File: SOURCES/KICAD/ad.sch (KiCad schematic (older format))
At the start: 178 parts, among them IC201 IC_OPA1652AIDR, IC202 IC_OPA1652AIDR, IC203 IC_OPA1652AIDR, IC204 IC_OPA1652AIDR, IC205 IC_AK5558VN, IC206 IC_OPA1652AIDR, IC207 IC_OPA1652AIDR, IC208 IC_OPA1652AIDR, IC209 IC_OPA1652AIDR, X201 CONN_02X13

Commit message: I2C control of ADC
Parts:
- removed R216: RES_0R00_1%_0.125W_Thick_0805, rklib:C0805-RES, symbol rk:RES_0R00_1%_0.125W_Thick_0805
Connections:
- net +3V3: now also IC205.44 (CKS1/CAD0_I2C/CSN), IC205.48 (SD/PMOD), IC205.52 (TDM1), IC205.56 (DCKS/HPFE); no longer IC205.53 (PSN/CAD0_SPI), R213.1, R214.1, R225.1, R226.1
- net GND: now also IC205.46 (CKS3/CAD1), IC205.47 (SLOW/DCKB), IC205.49 (DIF0), IC205.50 (DIF1), IC205.51 (TDM0), IC205.53 (PSN/CAD0_SPI); no longer R215.1, R217.1, R235.2, R236.2, R237.2
- net at R237.1: no longer IC205.43 (CKS0/SDA/CDTI)
- net at R227.2: no longer IC205.44 (CKS1/CAD0_I2C/CSN)
- net at R226.2: no longer IC205.45 (CKS2/SCL/CCLK)
- net at R236.1: no longer IC205.46 (CKS3/CAD1)
- net at R235.1: no longer IC205.47 (SLOW/DCKB)
- net at R225.2: no longer IC205.48 (SD/PMOD)
- net at R217.2: no longer IC205.49 (DIF0)
- net at R215.2: no longer IC205.51 (TDM0)
- net at R214.2: no longer IC205.52 (TDM1)
- net at R213.2: no longer IC205.56 (DCKS/HPFE)
- new net SCL: IC205.45 (CKS2/SCL/CCLK)
- new net SDA: IC205.43 (CKS0/SDA/CDTI)
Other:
- note added: "I2C addr: 0x22/0x23"
- note removed: "Resistors are only for\nprototype"
- moved on the sheet: R213, R214, R215, R217, R225, R226, R235, R236, R237, X201

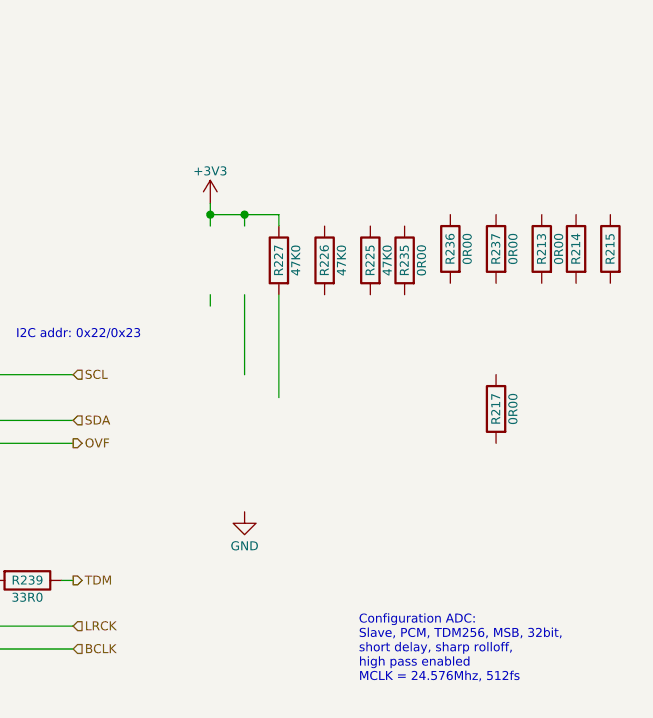
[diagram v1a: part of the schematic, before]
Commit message: I2C control of DAC
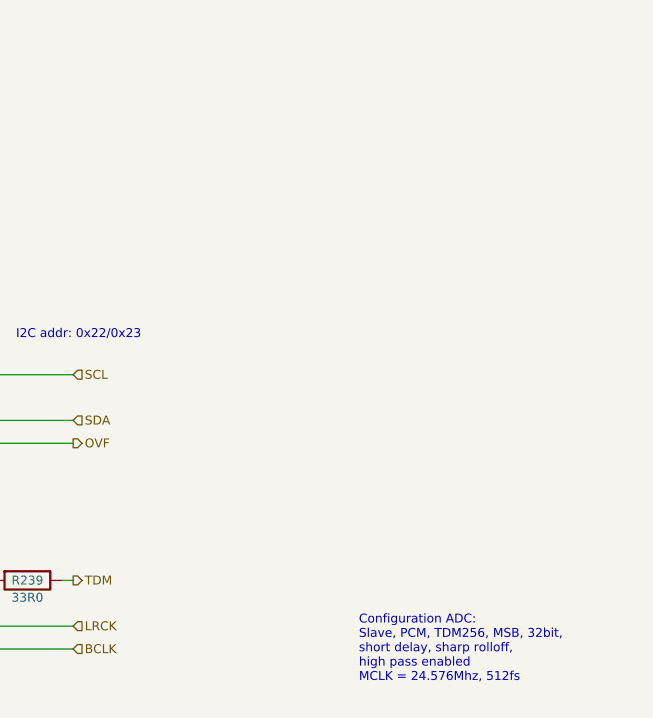
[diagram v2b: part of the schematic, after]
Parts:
- removed R213, R214, R215, R217, R235, R236, R237: RES_0R00_1%_0.125W_Thick_0805, rklib:C0805-RES, symbol rk:RES_0R00_1%_0.125W_Thick_0805
- removed R225, R226, R227: RES_47K0_1%_0.125W_Thick_0805, rklib:C0805-RES, symbol rk:RES_47K0_1%_0.125W_Thick_0805
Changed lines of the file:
@@
 Text HLabel 13250 5400 2    39   Output ~ 0
 OVF
-$Comp
-L freeDSP-aurora-rescue:+3V3 #PWR0135
-U 1 1 59094BBE
-P 13850 4350
-F 0 "#PWR0135" H 13850 4200 50  0001 C CNN
-F 1 "+3V3" H 13850 4490 39  0000 C CNN
-F 2 "" H 13850 4350 50  0000 C CNN
-F 3 "" H 13850 4350 50  0000 C CNN
-	1    13850 4350
-	1    0    0    -1
-$EndComp
 Connection ~ 4400 2000
 Wire Wire Line
@@
 Wire Wire Line
 	12750 5400 13250 5400
-Wire Wire Line
-	13850 4800 13850 4750
-Wire Wire Line
-	13850 4350 13850 4400
-Wire Wire Line
-	13850 4400 14000 4400
-Connection ~ 13850 4400
 Text HLabel 12000 6800 3    39   Input ~ 0
 ~RST
@@
 NoConn ~ 12750 5600
 NoConn ~ 12750 5500
-$Comp
-L freeDSP-aurora-rescue:GND #PWR0139
-U 1 1 5909BFB0
-P 14000 5700
-F 0 "#PWR0139" H 14000 5450 50  0001 C CNN
-F 1 "GND" H 14000 5550 39  0000 C CNN
-F 2 "" H 14000 5700 50  0000 C CNN
-F 3 "" H 14000 5700 50  0000 C CNN
-	1    14000 5700
-	1    0    0    -1
-$EndComp
-Wire Wire Line
-	14000 4400 14000 4450
-Wire Wire Line
-	14150 4400 14150 4450
-Connection ~ 14000 4400
-Wire Wire Line
-	14000 4750 14000 5100
-Wire Wire Line
-	14150 4750 14150 5200
 Wire Wire Line
 	12750 5300 13250 5300
@@
 Wire Wire Line
 	11500 4400 11800 4400
-Wire Wire Line
-	13850 4400 13850 4450
-Wire Wire Line
-	14000 4400 14150 4400
 Wire Wire Line
 	1400 5350 1400 5500
@@
 $EndComp
 $Comp
-L rk:RES_47K0_1%_0.125W_Thick_0805 R225
-U 1 1 5F563855
-P 14550 4600
-F 0 "R225" H 14550 4600 39  0000 C CNN
-F 1 "RES_47K0_1%_0.125W_Thick_0805" H 14550 4425 39  0001 C CNN
-F 2 "rklib:C0805-RES" H 14550 4375 39  0001 C CNN
-F 3 "" H 14550 4600 50  0000 C CNN
-F 4 "47K0" H 14550 4525 39  0000 C CNN "Value1"
-F 5 "1% 0.125W Thick" H 14550 4475 39  0001 C CNN "Value2"
-F 6 "311-47.0KCRCT-ND" H 14550 4300 39  0001 C CNN "digikey"
-F 7 "Yageo" H 700 0   50  0001 C CNN "Manufacturer"
-F 8 "RC0805FR-0747KL" H 700 0   50  0001 C CNN "pn"
-	1    14550 4600
-	0    -1   1    0
-$EndComp
-$Comp
-L rk:RES_0R00_1%_0.125W_Thick_0805 R235
-U 1 1 5F563B37
-P 14700 4600
-F 0 "R235" H 14700 4600 39  0000 C CNN
-F 1 "RES_0R00_1%_0.125W_Thick_0805" H 14700 4425 39  0001 C CNN
-F 2 "rklib:C0805-RES" H 14700 4375 39  0001 C CNN
-F 3 "" H 14700 4600 50  0000 C CNN
-F 4 "0R00" H 14700 4525 39  0000 C CNN "Value1"
-F 5 "1% 0.125W Thick" H 14700 4475 39  0001 C CNN "Value2"
-F 6 "311-0.0ARCT-ND" H 14700 4300 39  0001 C CNN "digikey"
-F 7 "Yageo" H 1000 -950 50  0001 C CNN "Manufacturer"
-F 8 "RC0805JR-070RL" H 1000 -950 50  0001 C CNN "pn"
-	1    14700 4600
-	0    -1   1    0
-$EndComp
-$Comp
-L rk:RES_47K0_1%_0.125W_Thick_0805 R226
-U 1 1 5F6AECFA
-P 14350 4600
-F 0 "R226" H 14350 4600 39  0000 C CNN
-F 1 "RES_47K0_1%_0.125W_Thick_0805" H 14350 4425 39  0001 C CNN
-F 2 "rklib:C0805-RES" H 14350 4375 39  0001 C CNN
-F 3 "" H 14350 4600 50  0000 C CNN
-F 4 "47K0" H 14350 4525 39  0000 C CNN "Value1"
-F 5 "1% 0.125W Thick" H 14350 4475 39  0001 C CNN "Value2"
-F 6 "311-47.0KCRCT-ND" H 14350 4300 39  0001 C CNN "digikey"
-F 7 "Yageo" H 350 0   50  0001 C CNN "Manufacturer"
-F 8 "RC0805FR-0747KL" H 350 0   50  0001 C CNN "pn"
-	1    14350 4600
-	0    -1   1    0
-$EndComp
-$Comp
-L rk:RES_47K0_1%_0.125W_Thick_0805 R227
-U 1 1 5F6E5CCB
-P 14150 4600
-F 0 "R227" H 14150 4600 39  0000 C CNN
-F 1 "RES_47K0_1%_0.125W_Thick_0805" H 14150 4425 39  0001 C CNN
-F 2 "rklib:C0805-RES" H 14150 4375 39  0001 C CNN
-F 3 "" H 14150 4600 50  0000 C CNN
-F 4 "47K0" H 14150 4525 39  0000 C CNN "Value1"
-F 5 "1% 0.125W Thick" H 14150 4475 39  0001 C CNN "Value2"
-F 6 "311-47.0KCRCT-ND" H 14150 4300 39  0001 C CNN "digikey"
-F 7 "Yageo" H 0   0   50  0001 C CNN "Manufacturer"
-F 8 "RC0805FR-0747KL" H 0   0   50  0001 C CNN "pn"
-	1    14150 4600
-	0    -1   1    0
-$EndComp
-$Comp
-L rk:RES_0R00_1%_0.125W_Thick_0805 R236
-U 1 1 5F7550E4
-P 14900 4550
-F 0 "R236" H 14900 4550 39  0000 C CNN
-F 1 "RES_0R00_1%_0.125W_Thick_0805" H 14900 4375 39  0001 C CNN
-F 2 "rklib:C0805-RES" H 14900 4325 39  0001 C CNN
-F 3 "" H 14900 4550 50  0000 C CNN
-F 4 "0R00" H 14900 4475 39  0000 C CNN "Value1"
-F 5 "1% 0.125W Thick" H 14900 4425 39  0001 C CNN "Value2"
-F 6 "311-0.0ARCT-ND" H 14900 4250 39  0001 C CNN "digikey"
-F 7 "Yageo" H 1050 -1000 50  0001 C CNN "Manufacturer"
-F 8 "RC0805JR-070RL" H 1050 -1000 50  0001 C CNN "pn"
-	1    14900 4550
-	0    -1   1    0
-$EndComp
-$Comp
-L rk:RES_0R00_1%_0.125W_Thick_0805 R237
-U 1 1 5F78C0BA
-P 15100 4550
-F 0 "R237" H 15100 4550 39  0000 C CNN
-F 1 "RES_0R00_1%_0.125W_Thick_0805" H 15100 4375 39  0001 C CNN
-F 2 "rklib:C0805-RES" H 15100 4325 39  0001 C CNN
-F 3 "" H 15100 4550 50  0000 C CNN
-F 4 "0R00" H 15100 4475 39  0000 C CNN "Value1"
-F 5 "1% 0.125W Thick" H 15100 4425 39  0001 C CNN "Value2"
-F 6 "311-0.0ARCT-ND" H 15100 4250 39  0001 C CNN "digikey"
-F 7 "Yageo" H 1100 -1000 50  0001 C CNN "Manufacturer"
-F 8 "RC0805JR-070RL" H 1100 -1000 50  0001 C CNN "pn"
-	1    15100 4550
-	0    -1   1    0
-$EndComp
-$Comp
-L rk:RES_0R00_1%_0.125W_Thick_0805 R214
-U 1 1 5F7C3863
-P 15450 4550
-F 0 "R214" H 15450 4550 39  0000 C CNN
-F 1 "RES_0R00_1%_0.125W_Thick_0805" H 15450 4375 39  0001 C CNN
-F 2 "rklib:C0805-RES" H 15450 4325 39  0001 C CNN
-F 3 "" H 15450 4550 50  0000 C CNN
-F 4 "0R00" H 15450 4475 39  0001 C CNN "Value1"
-F 5 "1% 0.125W Thick" H 15450 4425 39  0001 C CNN "Value2"
-F 6 "311-0.0ARCT-ND" H 15450 4250 39  0001 C CNN "digikey"
-F 7 "Yageo" H 3350 400 50  0001 C CNN "Manufacturer"
-F 8 "RC0805JR-070RL" H 3350 400 50  0001 C CNN "pn"
-	1    15450 4550
-	0    -1   1    0
-$EndComp
-$Comp
-L rk:RES_0R00_1%_0.125W_Thick_0805 R213
-U 1 1 5F8323C2
-P 15300 4550
-F 0 "R213" H 15300 4550 39  0000 C CNN
-F 1 "RES_0R00_1%_0.125W_Thick_0805" H 15300 4375 39  0001 C CNN
-F 2 "rklib:C0805-RES" H 15300 4325 39  0001 C CNN
-F 3 "" H 15300 4550 50  0000 C CNN
-F 4 "0R00" H 15300 4475 39  0000 C CNN "Value1"
-F 5 "1% 0.125W Thick" H 15300 4425 39  0001 C CNN "Value2"
-F 6 "311-0.0ARCT-ND" H 15300 4250 39  0001 C CNN "digikey"
-F 7 "Yageo" H 3600 400 50  0001 C CNN "Manufacturer"
-F 8 "RC0805JR-070RL" H 3600 400 50  0001 C CNN "pn"
-	1    15300 4550
-	0    -1   1    0
-$EndComp
-$Comp
-L rk:RES_0R00_1%_0.125W_Thick_0805 R215
-U 1 1 5F86A287
-P 15600 4550
-F 0 "R215" H 15600 4550 39  0000 C CNN
-F 1 "RES_0R00_1%_0.125W_Thick_0805" H 15600 4375 39  0001 C CNN
-F 2 "rklib:C0805-RES" H 15600 4325 39  0001 C CNN
-F 3 "" H 15600 4550 50  0000 C CNN
-F 4 "0R00" H 15600 4475 39  0001 C CNN "Value1"
-F 5 "1% 0.125W Thick" H 15600 4425 39  0001 C CNN "Value2"
-F 6 "311-0.0ARCT-ND" H 15600 4250 39  0001 C CNN "digikey"
-F 7 "Yageo" H 3400 400 50  0001 C CNN "Manufacturer"
-F 8 "RC0805JR-070RL" H 3400 400 50  0001 C CNN "pn"
-	1    15600 4550
-	0    -1   1    0
-$EndComp
-$Comp
-L rk:RES_0R00_1%_0.125W_Thick_0805 R217
-U 1 1 5F8D821F
-P 15100 5250
-F 0 "R217" H 15100 5250 39  0000 C CNN
-F 1 "RES_0R00_1%_0.125W_Thick_0805" H 15100 5075 39  0001 C CNN
-F 2 "rklib:C0805-RES" H 15100 5025 39  0001 C CNN
-F 3 "" H 15100 5250 50  0000 C CNN
-F 4 "0R00" H 15100 5175 39  0000 C CNN "Value1"
-F 5 "1% 0.125W Thick" H 15100 5125 39  0001 C CNN "Value2"
-F 6 "311-0.0ARCT-ND" H 15100 4950 39  0001 C CNN "digikey"
-F 7 "Yageo" H 2700 1100 50  0001 C CNN "Manufacturer"
-F 8 "RC0805JR-070RL" H 2700 1100 50  0001 C CNN "pn"
-	1    15100 5250
-	0    -1   1    0
-$EndComp
-$Comp

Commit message: Optimized ground plane
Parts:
- X201: footprint rklib:HDR_02x13 -> rklib:IDC26; symbol freeDSP-aurora-rescue:CONN_02X13 -> rk:CON_IDC26
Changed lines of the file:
@@
 	1    0    0    -1
 $EndComp
-Text Notes 14500 6450 0    39   ~ 0
+Text Notes 14250 5650 0    39   ~ 0
 Configuration ADC:\nSlave, PCM, TDM256, MSB, 32bit,\nshort delay, sharp rolloff,\nhigh pass enabled\nMCLK = 24.576Mhz, 512fs
 Text HLabel 13250 6000 2    39   Output ~ 0
@@
 NoConn ~ 12750 5800
 NoConn ~ 12750 5700
-Text Notes 13000 4950 0    39   ~ 0
+Text Notes 14250 5750 0    39   ~ 0
 I2C addr: 0x22/0x23
 Text HLabel 13250 5400 2    39   Output ~ 0
@@
 	12750 5300 13250 5300
 $Comp
-L freeDSP-aurora-rescue:CONN_02X13 X201
+L rk:CON_IDC26 X201
 U 1 1 590CECF6
 P 1100 4850
 F 0 "X201" H 1100 5550 39  0000 C CNN
 F 1 "CONN_02X13" V 1100 4850 39  0000 C CNN
-F 2 "rklib:HDR_02x13" H 1100 3700 50  0001 C CNN
+F 2 "rklib:IDC26" H 1100 3700 50  0001 C CNN
 F 3 "" H 1100 3700 50  0000 C CNN
 F 4 "SKT_02x13" H -300 -1150 50  0001 C CNN "Value1"
@@
 L freeDSP-aurora-rescue:GND #PWR0140
 U 1 1 590CECFD
-P 1400 5500
-F 0 "#PWR0140" H 1400 5250 50  0001 C CNN
-F 1 "GND" H 1400 5350 39  0000 C CNN
-F 2 "" H 1400 5500 50  0000 C CNN
-F 3 "" H 1400 5500 50  0000 C CNN
-	1    1400 5500
+P 1350 5500
+F 0 "#PWR0140" H 1350 5250 50  0001 C CNN
+F 1 "GND" H 1350 5350 39  0000 C CNN
+F 2 "" H 1350 5500 50  0000 C CNN
+F 3 "" H 1350 5500 50  0000 C CNN
+	1    1350 5500
 	1    0    0    -1
 $EndComp
@@
 L freeDSP-aurora-rescue:GND #PWR0141
 U 1 1 590CED03
-P 800 5500
-F 0 "#PWR0141" H 800 5250 50  0001 C CNN
-F 1 "GND" H 800 5350 39  0000 C CNN
-F 2 "" H 800 5500 50  0000 C CNN
-F 3 "" H 800 5500 50  0000 C CNN
-	1    800  5500
+P 850 5500
+F 0 "#PWR0141" H 850 5250 50  0001 C CNN
+F 1 "GND" H 850 5350 39  0000 C CNN
+F 2 "" H 850 5500 50  0000 C CNN
+F 3 "" H 850 5500 50  0000 C CNN
+	1    850  5500
 	1    0    0    -1
 $EndComp
 Wire Wire Line
-	1400 5350 1350 5350
-Wire Wire Line
-	1400 4450 1400 4750
-Wire Wire Line
-	1350 5050 1400 5050
-Connection ~ 1400 5350
-Wire Wire Line
-	1350 4750 1400 4750
-Connection ~ 1400 5050
-Wire Wire Line
-	1350 4450 1400 4450
-Connection ~ 1400 4750
-Wire Wire Line
-	800  5250 850  5250
-Wire Wire Line
-	800  4350 800  4650
-Wire Wire Line
-	850  4950 800  4950
-Connection ~ 800  5250
-Wire Wire Line
-	850  4650 800  4650
-Connection ~ 800  4950
-Wire Wire Line
-	850  4350 800  4350
-Connection ~ 800  4650
-Wire Wire Line
-	850  5350 550  5350
-Text Label 550  5350 0    39   ~ 0
+	1350 5350 1300 5350
+Wire Wire Line
+	1350 4450 1350 4750
+Wire Wire Line
+	1300 5050 1350 5050
+Connection ~ 1350 5350
+Wire Wire Line
+	1300 4750 1350 4750
+Connection ~ 1350 5050
+Wire Wire Line
+	1300 4450 1350 4450
+Connection ~ 1350 4750
+Wire Wire Line
+	850  5250 900  5250
+Wire Wire Line
+	850  4350 850  4650
+Wire Wire Line
+	900  4950 850  4950
+Connection ~ 850  5250
+Wire Wire Line
+	900  4650 850  4650
+Connection ~ 850  4950
+Wire Wire Line
+	900  4350 850  4350
+Connection ~ 850  4650
+Wire Wire Line
+	900  5350 600  5350
+Text Label 600  5350 0    39   ~ 0
 AIN1-
-Text Label 1650 5250 2    39   ~ 0
+Text Label 1600 5250 2    39   ~ 0
 AIN1+
 Wire Wire Line
-	1350 5250 1650 5250
-Text Label 1650 5150 2    39   ~ 0
+	1300 5250 1600 5250
+Text Label 1600 5150 2    39   ~ 0
 AIN2-
 Wire Wire Line
-	1350 5150 1650 5150
-Text Label 1650 4950 2    39   ~ 0
+	1300 5150 1600 5150
+Text Label 1600 4950 2    39   ~ 0
 AIN3+
 Wire Wire Line
-	1350 4950 1650 4950
-Text Label 1650 4850 2    39   ~ 0
+	1300 4950 1600 4950
+Text Label 1600 4850 2    39   ~ 0
 AIN4-
 Wire Wire Line
-	1350 4850 1650 4850
-Text Label 1650 4650 2    39   ~ 0
+	1300 4850 1600 4850
+Text Label 1600 4650 2    39   ~ 0
 AIN5+
 Wire Wire Line
-	1350 4650 1650 4650
-Text Label 1650 4550 2    39   ~ 0
+	1300 4650 1600 4650
+Text Label 1600 4550 2    39   ~ 0
 AIN6-
 Wire Wire Line
-	1350 4550 1650 4550
-Text Label 1650 4350 2    39   ~ 0
+	1300 4550 1600 4550
+Text Label 1600 4350 2    39   ~ 0
 AIN7+
 Wire Wire Line
-	1350 4350 1650 4350
-Text Label 1650 4250 2    39   ~ 0
+	1300 4350 1600 4350
+Text Label 1600 4250 2    39   ~ 0
 AIN8-
 Wire Wire Line
-	1350 4250 1650 4250
-Wire Wire Line
-	850  5150 550  5150
-Text Label 550  5150 0    39   ~ 0
+	1300 4250 1600 4250
+Wire Wire Line
+	900  5150 600  5150
+Text Label 600  5150 0    39   ~ 0
 AIN2+
 Wire Wire Line
-	850  5050 550  5050
-Text Label 550  5050 0    39   ~ 0
+	900  5050 600  5050
+Text Label 600  5050 0    39   ~ 0
 AIN3-
 Wire Wire Line
-	850  4850 550  4850
-Text Label 550  4850 0    39   ~ 0
+	900  4850 600  4850
+Text Label 600  4850 0    39   ~ 0
 AIN4+
 Wire Wire Line
-	850  4750 550  4750
-Text Label 550  4750 0    39   ~ 0
+	900  4750 600  4750
+Text Label 600  4750 0    39   ~ 0
 AIN5-
 Wire Wire Line
-	850  4550 550  4550
-Text Label 550  4550 0    39   ~ 0
+	900  4550 600  4550
+Text Label 600  4550 0    39   ~ 0
 AIN6+
 Wire Wire Line
-	850  4450 550  4450
-Text Label 550  4450 0    39   ~ 0
+	900  4450 600  4450
+Text Label 600  4450 0    39   ~ 0
 AIN7-
 Wire Wire Line
-	850  4250 550  4250
-Text Label 550  4250 0    39   ~ 0
+	900  4250 600  4250
+Text Label 600  4250 0    39   ~ 0
 AIN8+
 Text HLabel 3850 3100 2    39   Input ~ 0
@@
 	11500 4400 11800 4400
 Wire Wire Line
-	1400 5350 1400 5500
-Wire Wire Line
-	1400 5050 1400 5350
-Wire Wire Line
-	1400 4750 1400 5050
-Wire Wire Line
-	800  5250 800  5500
-Wire Wire Line
-	800  4950 800  5250
-Wire Wire Line
-	800  4650 800  4950
+	1350 5350 1350 5500
+Wire Wire Line
+	1350 5050 1350 5350
+Wire Wire Line
+	1350 4750 1350 5050
+Wire Wire Line
+	850  5250 850  5500
+Wire Wire Line
+	850  4950 850  5250
+Wire Wire Line
+	850  4650 850  4950
 $Comp
 L rk:CAP_100n_50V_X7R_0805 C?

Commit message: Updated BOM
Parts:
- R201, R202, R209, R210, R219, R220, R231, R232, R240, R244, R249, R253, R254, R261, R262, R273: value RES_6K80_1%_0.25W_Thin_0805 -> RES_6K80_0.5%_0.125W_Thin_0805; Manufacturer (none) -> Panasonic Electronic Components; Value2 1% 0.25W Thin -> 0.5% 0.125W Thin; digikey (none) -> P6.6KBNCT-ND; pn (none) -> ERA-6AED682V
- R203, R204, R207, R208, R221, R222, R229, R230, R241, R243, R250, R252, R255, R256, R259, R260: Manufacturer (none) -> Stackpole Electronics Inc.; pn (none) -> RNCP0805FTD10K0
- R212, R233, R234, R245, R247, R263, R264, R265, R266, R267, R269, R271, R274, R275, R277, R279: value RES_2K20_1%_0.25W_Thin_0805 -> RES_2K20_0.5%_0.125W_Thin_0805; Manufacturer (none) -> Panasonic Electronic Components; Value2 1% 0.25W Thin -> 0.5% 0.125W Thin; digikey (none) -> P2.2KBNCT-ND; pn (none) -> ERA-6AED222V
- X201: value CONN_02X13 -> CON_IDC26; Manufacturer Sullins Connector Solutions -> Bud Industries; Value1 SKT_02x13 -> IDC26; digikey ??? -> 377-2269-ND; pn PRPC013DAAN-RC -> BC-32677
